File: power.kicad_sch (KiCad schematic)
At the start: 42 parts, among them U5 RT8097AHGE, U6 RT8097AHGE, U7 RT9080-28GJ5, U8 RT9080-18GJ5, U9 RT9080-12GJ5

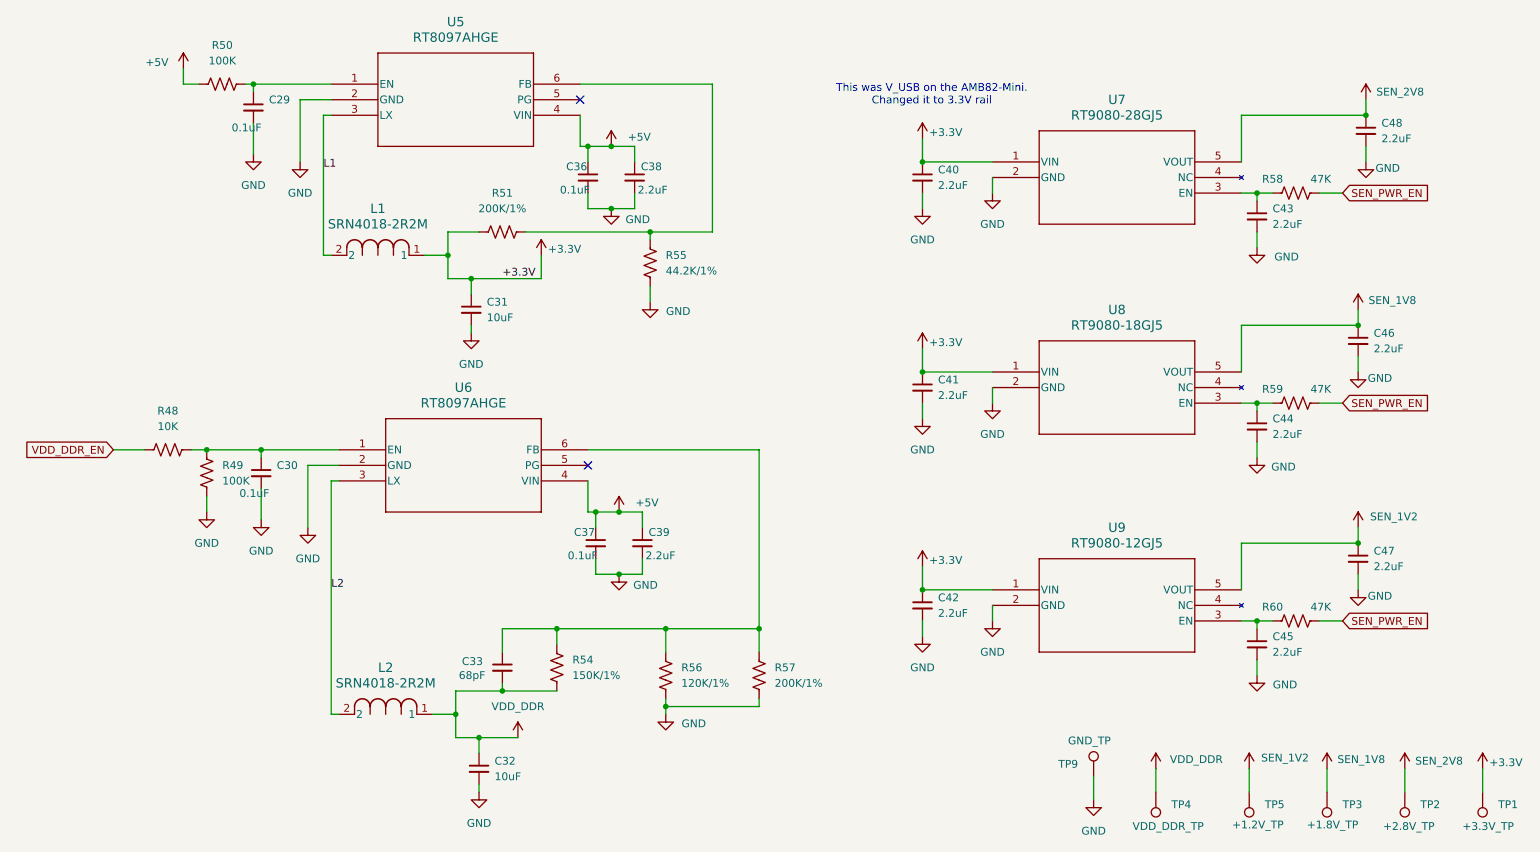
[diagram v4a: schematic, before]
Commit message: Replaced all passive footprints from 0603 metric to 0603 imperial. Big oversight. All done. Next is DRC
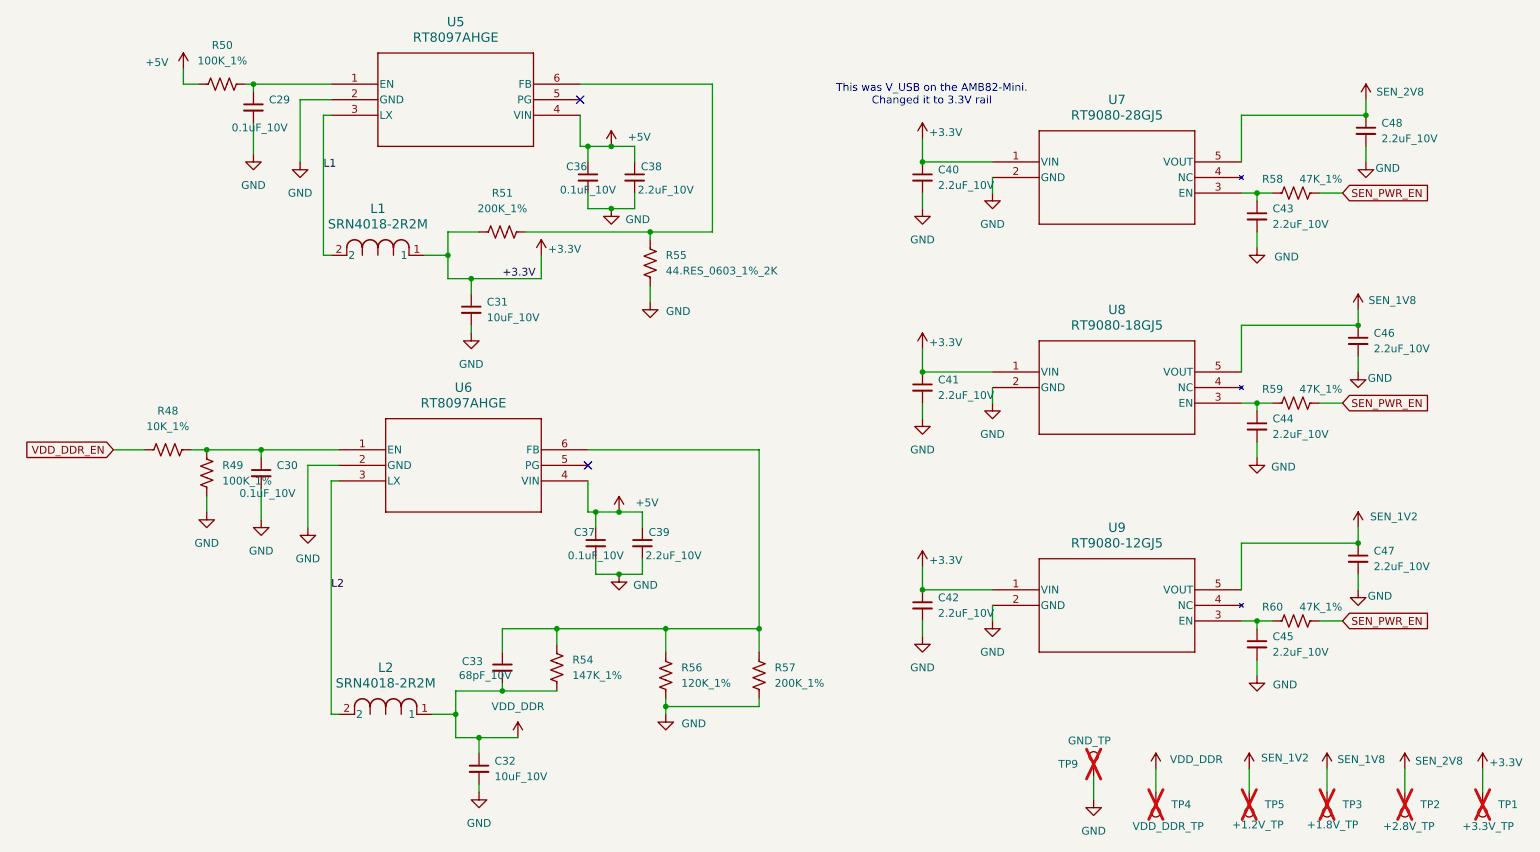
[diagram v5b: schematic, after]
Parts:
- C29, C30, C36, C37: value 0.1uF -> 0.1uF_10V; footprint Capacitor_SMD:C_0201_0603Metric_Pad0.64x0.40mm_HandSolder -> Capacitor_SMD:C_0603_1608Metric
- C31, C32: value 10uF -> 10uF_10V; footprint Capacitor_SMD:C_0201_0603Metric_Pad0.64x0.40mm_HandSolder -> Capacitor_SMD:C_0603_1608Metric
- C33: value 68pF -> 68pF_10V; footprint Capacitor_SMD:C_0201_0603Metric_Pad0.64x0.40mm_HandSolder -> Capacitor_SMD:C_0603_1608Metric
- C38, C39, C40, C41, C42, C43, C44, C45, C46, C47, C48: value 2.2uF -> 2.2uF_10V; footprint Capacitor_SMD:C_0201_0603Metric_Pad0.64x0.40mm_HandSolder -> Capacitor_SMD:C_0603_1608Metric
- R48: value 10K -> 10K_1%; footprint Resistor_SMD:R_0201_0603Metric_Pad0.64x0.40mm_HandSolder -> Resistor_SMD:R_0603_1608Metric
- R49, R50: value 100K -> 100K_1%; footprint Resistor_SMD:R_0201_0603Metric_Pad0.64x0.40mm_HandSolder -> Resistor_SMD:R_0603_1608Metric
- R51, R57: value 200K/1% -> 200K_1%; footprint Resistor_SMD:R_0201_0603Metric_Pad0.64x0.40mm_HandSolder -> Resistor_SMD:R_0603_1608Metric
- R54: value 150K/1% -> 147K_1%; footprint Resistor_SMD:R_0201_0603Metric_Pad0.64x0.40mm_HandSolder -> Resistor_SMD:R_0603_1608Metric
- R55: value 44.2K/1% -> 44.RES_0603_1%_2K; footprint Resistor_SMD:R_0201_0603Metric_Pad0.64x0.40mm_HandSolder -> Resistor_SMD:R_0603_1608Metric
- R56: value 120K/1% -> 120K_1%; footprint Resistor_SMD:R_0201_0603Metric_Pad0.64x0.40mm_HandSolder -> Resistor_SMD:R_0603_1608Metric
- R58, R59, R60: value 47K -> 47K_1%; footprint Resistor_SMD:R_0201_0603Metric_Pad0.64x0.40mm_HandSolder -> Resistor_SMD:R_0603_1608Metric
- TP1, TP2, TP3, TP4, TP5, TP9: now not fitted
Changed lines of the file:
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@@
 			)
 		)
-		(property "Value" "0.1uF"
+		(property "Value" "0.1uF_10V"
 			(at 51.054 101.092 0)
 			(effects
@@
 			)
 		)
-		(property "Footprint" "Capacitor_SMD:C_0201_0603Metric_Pad0.64x0.40mm_HandSolder"
+		(property "Footprint" "Capacitor_SMD:C_0603_1608Metric"
 			(at 54.61 97.79 0)
 			(effects
@@
 		(in_bom yes)
 		(on_board yes)
-		(dnp no)
+		(dnp yes)
 		(property "Reference" "TP2"
 			(at 243.84 151.8919 0)
@@
 			)
 		)
-		(property "Value" "2.2uF"
+		(property "Value" "2.2uF_10V"
 			(at 116.078 51.562 0)
 			(effects
@@
 			)
 		)
-		(property "Footprint" "Capacitor_SMD:C_0201_0603Metric_Pad0.64x0.40mm_HandSolder"
+		(property "Footprint" "Capacitor_SMD:C_0603_1608Metric"
 			(at 115.57 49.53 0)
 			(effects
@@
 		(in_bom yes)
 		(on_board yes)
-		(dnp no)
+		(dnp yes)
 		(property "Reference" "TP5"
 			(at 218.44 151.8919 0)
@@
 			)
 		)
-		(property "Value" "2.2uF"
+		(property "Value" "2.2uF_10V"
 			(at 237.49 43.1862 0)
 			(effects
@@
 			)
 		)
-		(property "Footprint" "Capacitor_SMD:C_0201_0603Metric_Pad0.64x0.40mm_HandSolder"
+		(property "Footprint" "Capacitor_SMD:C_0603_1608Metric"
 			(at 234.95 41.91 0)
 			(effects
@@
 			)
 		)
-		(property "Value" "2.2uF"
+		(property "Value" "2.2uF_10V"
 			(at 219.71 91.4462 0)
 			(effects
@@
 			)
 		)
-		(property "Footprint" "Capacitor_SMD:C_0201_0603Metric_Pad0.64x0.40mm_HandSolder"
+		(property "Footprint" "Capacitor_SMD:C_0603_1608Metric"
 			(at 217.17 90.17 0)
 			(effects
@@
 			)
 		)
-		(property "Value" "2.2uF"
+		(property "Value" "2.2uF_10V"
 			(at 236.22 113.0362 0)
 			(effects
@@
 			)
 		)
-		(property "Footprint" "Capacitor_SMD:C_0201_0603Metric_Pad0.64x0.40mm_HandSolder"
+		(property "Footprint" "Capacitor_SMD:C_0603_1608Metric"
 			(at 233.68 111.76 0)
 			(effects
@@
 			)
 		)
-		(property "Value" "10uF"
+		(property "Value" "10uF_10V"
 			(at 92.71 147.3262 0)
 			(effects
@@
 			)
 		)
-		(property "Footprint" "Capacitor_SMD:C_0201_0603Metric_Pad0.64x0.40mm_HandSolder"
+		(property "Footprint" "Capacitor_SMD:C_0603_1608Metric"
 			(at 90.17 146.05 0)
 			(effects
@@
 			)
 		)
-		(property "Value" "2.2uF"
+		(property "Value" "2.2uF_10V"
 			(at 165.1 50.8062 0)
 			(effects
@@
 			)
 		)
-		(property "Footprint" "Capacitor_SMD:C_0201_0603Metric_Pad0.64x0.40mm_HandSolder"
+		(property "Footprint" "Capacitor_SMD:C_0603_1608Metric"
 			(at 162.56 49.53 0)
 			(effects
@@
 		(in_bom yes)
 		(on_board yes)
-		(dnp no)
+		(dnp yes)
 		(property "Reference" "TP1"
 			(at 256.54 151.8919 0)
@@
 		(in_bom yes)
 		(on_board yes)
-		(dnp no)
+		(dnp yes)
 		(property "Reference" "TP9"
 			(at 187.96 145.2881 0)
@@
 			)
 		)
-		(property "Value" "2.2uF"
+		(property "Value" "2.2uF_10V"
 			(at 165.1 120.6562 0)
 			(effects
@@
 			)
 		)
-		(property "Footprint" "Capacitor_SMD:C_0201_0603Metric_Pad0.64x0.40mm_HandSolder"
+		(property "Footprint" "Capacitor_SMD:C_0603_1608Metric"
 			(at 162.56 119.38 0)
 			(effects
@@
 			)
 		)
-		(property "Value" "100K"
+		(property "Value" "100K_1%"
 			(at 48.26 30.48 90)
 			(effects
@@
 			)
 		)
-		(property "Footprint" "Resistor_SMD:R_0201_0603Metric_Pad0.64x0.40mm_HandSolder"
+		(property "Footprint" "Resistor_SMD:R_0603_1608Metric"
 			(at 48.514 33.274 90)
 			(effects
@@
 			)
 		)
-		(property "Value" "0.1uF"
+		(property "Value" "0.1uF_10V"
 			(at 103.378 51.562 0)
 			(effects
@@
 			)
 		)
-		(property "Footprint" "Capacitor_SMD:C_0201_0603Metric_Pad0.64x0.40mm_HandSolder"
+		(property "Footprint" "Capacitor_SMD:C_0603_1608Metric"
 			(at 107.95 49.53 0)
 			(effects
@@
 			)
 		)
-		(property "Value" "100K"
+		(property "Value" "100K_1%"
 			(at 48.26 99.0599 0)
 			(effects
@@
 			)
 		)
-		(property "Footprint" "Resistor_SMD:R_0201_0603Metric_Pad0.64x0.40mm_HandSolder"
+		(property "Footprint" "Resistor_SMD:R_0603_1608Metric"
 			(at 44.704 97.536 90)
 			(effects
@@
 			)
 		)
-		(property "Value" "150K/1%"
+		(property "Value" "147K_1%"
 			(at 105.41 130.8099 0)
 			(effects
@@
 			)
 		)
-		(property "Footprint" "Resistor_SMD:R_0201_0603Metric_Pad0.64x0.40mm_HandSolder"
+		(property "Footprint" "Resistor_SMD:R_0603_1608Metric"
 			(at 101.854 129.286 90)
 			(effects
@@
 		(in_bom yes)
 		(on_board yes)
-		(dnp no)
+		(dnp yes)
 		(property "Reference" "TP4"
 			(at 203.2 151.8919 0)
@@
 		(in_bom yes)
 		(on_board yes)
-		(dnp no)
+		(dnp yes)
 		(property "Reference" "TP3"
 			(at 231.14 151.8919 0)
@@
 			)
 		)
-		(property "Value" "2.2uF"
+		(property "Value" "2.2uF_10V"
 			(at 165.1 85.0962 0)
 			(effects
@@
 			)
 		)
-		(property "Footprint" "Capacitor_SMD:C_0201_0603Metric_Pad0.64x0.40mm_HandSolder"
+		(property "Footprint" "Capacitor_SMD:C_0603_1608Metric"
 			(at 162.56 83.82 0)
 			(effects
@@
 			)
 		)
-		(property "Value" "44.2K/1%"
+		(property "Value" "44.RES_0603_1%_2K"
 			(at 120.65 64.7699 0)
 			(effects
@@
 			)
 		)
-		(property "Footprint" "Resistor_SMD:R_0201_0603Metric_Pad0.64x0.40mm_HandSolder"
+		(property "Footprint" "Resistor_SMD:R_0603_1608Metric"
 			(at 119.126 63.754 90)
 			(effects
@@
 			)
 		)
-		(property "Value" "47K"
+		(property "Value" "47K_1%"
 			(at 227.584 119.634 90)
 			(effects
@@
 			)
 		)
-		(property "Footprint" "Resistor_SMD:R_0201_0603Metric_Pad0.64x0.40mm_HandSolder"
+		(property "Footprint" "Resistor_SMD:R_0603_1608Metric"
 			(at 223.774 120.904 90)
 			(effects
@@
 			)
 		)
-		(property "Value" "2.2uF"
+		(property "Value" "2.2uF_10V"
 			(at 236.22 77.4762 0)
 			(effects
@@
 			)
 		)
-		(property "Footprint" "Capacitor_SMD:C_0201_0603Metric_Pad0.64x0.40mm_HandSolder"
+		(property "Footprint" "Capacitor_SMD:C_0603_1608Metric"
 			(at 233.68 76.2 0)
 			(effects
@@
 			)
 		)
-		(property "Value" "47K"
+		(property "Value" "47K_1%"
 			(at 227.584 49.784 90)
 			(effects
@@
 			)
 		)
-		(property "Footprint" "Resistor_SMD:R_0201_0603Metric_Pad0.64x0.40mm_HandSolder"
+		(property "Footprint" "Resistor_SMD:R_0603_1608Metric"
 			(at 223.774 51.054 90)
 			(effects
@@
 			)
 		)
-		(property "Value" "10uF"
+		(property "Value" "10uF_10V"
 			(at 91.44 72.3962 0)
 			(effects
@@
 			)
 		)
-		(property "Footprint" "Capacitor_SMD:C_0201_0603Metric_Pad0.64x0.40mm_HandSolder"
+		(property "Footprint" "Capacitor_SMD:C_0603_1608Metric"
 			(at 88.9 71.12 0)
 			(effects
@@
 			)
 		)
-		(property "Value" "2.2uF"
+		(property "Value" "2.2uF_10V"
 			(at 219.71 57.1562 0)
 			(effects
@@
 			)
 		)
-		(property "Footprint" "Capacitor_SMD:C_0201_0603Metric_Pad0.64x0.40mm_HandSolder"
+		(property "Footprint" "Capacitor_SMD:C_0603_1608Metric"
 			(at 217.17 55.88 0)
 			(effects
@@
 			)
 		)
-		(property "Value" "0.1uF"
+		(property "Value" "0.1uF_10V"
 			(at 49.784 41.402 0)
 			(effects
@@
 			)
 		)
-		(property "Footprint" "Capacitor_SMD:C_0201_0603Metric_Pad0.64x0.40mm_HandSolder"
+		(property "Footprint" "Capacitor_SMD:C_0603_1608Metric"
 			(at 53.34 38.1 0)
 			(effects
@@
 			)
 		)
-		(property "Value" "2.2uF"
+		(property "Value" "2.2uF_10V"
 			(at 219.71 127.0062 0)
 			(effects
@@
 			)
 		)
-		(property "Footprint" "Capacitor_SMD:C_0201_0603Metric_Pad0.64x0.40mm_HandSolder"
+		(property "Footprint" "Capacitor_SMD:C_0603_1608Metric"
 			(at 217.17 125.73 0)
 			(effects
@@
 			)
 		)
-		(property "Value" "47K"
+		(property "Value" "47K_1%"
 			(at 227.584 84.074 90)
 			(effects
@@
 			)
 		)
-		(property "Footprint" "Resistor_SMD:R_0201_0603Metric_Pad0.64x0.40mm_HandSolder"
+		(property "Footprint" "Resistor_SMD:R_0603_1608Metric"
 			(at 223.774 85.344 90)
 			(effects
@@
 			)
 		)
-		(property "Value" "200K/1%"
+		(property "Value" "200K_1%"
 			(at 93.98 54.61 90)
 			(effects
@@
 			)
 		)
-		(property "Footprint" "Resistor_SMD:R_0201_0603Metric_Pad0.64x0.40mm_HandSolder"
+		(property "Footprint" "Resistor_SMD:R_0603_1608Metric"
 			(at 94.234 57.404 90)
 			(effects
@@
 			)
 		)
-		(property "Value" "10K"
+		(property "Value" "10K_1%"
 			(at 39.37 90.17 90)
 			(effects
@@
 			)
 		)
-		(property "Footprint" "Resistor_SMD:R_0201_0603Metric_Pad0.64x0.40mm_HandSolder"
+		(property "Footprint" "Resistor_SMD:R_0603_1608Metric"
 			(at 39.624 92.964 90)
 			(effects
@@
 			)
 		)
-		(property "Value" "2.2uF"
+		(property "Value" "2.2uF_10V"
 			(at 117.348 111.252 0)
 			(effects
@@
 			)
 		)
-		(property "Footprint" "Capacitor_SMD:C_0201_0603Metric_Pad0.64x0.40mm_HandSolder"
+		(property "Footprint" "Capacitor_SMD:C_0603_1608Metric"
 			(at 116.84 109.22 0)
 			(effects
@@
 			)
 		)
-		(property "Value" "0.1uF"
+		(property "Value" "0.1uF_10V"
 			(at 104.648 111.252 0)
 			(effects
@@
 			)
 		)
-		(property "Footprint" "Capacitor_SMD:C_0201_0603Metric_Pad0.64x0.40mm_HandSolder"
+		(property "Footprint" "Capacitor_SMD:C_0603_1608Metric"
 			(at 109.22 109.22 0)
 			(effects
@@
 			)
 		)
-		(property "Value" "120K/1%"
+		(property "Value" "120K_1%"
 			(at 123.19 132.0799 0)
 			(effects
@@
 			)
 		)
-		(property "Footprint" "Resistor_SMD:R_0201_0603Metric_Pad0.64x0.40mm_HandSolder"
+		(property "Footprint" "Resistor_SMD:R_0603_1608Metric"
 			(at 121.666 131.064 90)
 			(effects
@@
 			)
 		)
-		(property "Value" "68pF"
+		(property "Value" "68pF_10V"
 			(at 86.868 130.81 0)
 			(effects
@@
 			)
 		)
-		(property "Footprint" "Capacitor_SMD:C_0201_0603Metric_Pad0.64x0.40mm_HandSolder"
+		(property "Footprint" "Capacitor_SMD:C_0603_1608Metric"
 			(at 93.98 129.54 0)
 			(effects
@@
 			)
 		)
-		(property "Value" "200K/1%"
+		(property "Value" "200K_1%"
 			(at 138.43 132.0799 0)
 			(effects
@@
 			)
 		)
-		(property "Footprint" "Resistor_SMD:R_0201_0603Metric_Pad0.64x0.40mm_HandSolder"
+		(property "Footprint" "Resistor_SMD:R_0603_1608Metric"
 			(at 136.906 131.064 90)
 			(effects

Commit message: All fiducials and mounting holes placed. Except one hole, which I'll try to place. WIP
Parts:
- L1, L2: footprint IND_BOURNS_SRN4018 -> SRN4018-2R2M:IND_BOURNS_SRN4018
- U7, U8, U9: footprint TSOT-23-5_RIT -> RTL9080:TSOT-23-5_RIT
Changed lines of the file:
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@@
 			)
 		)
-		(property "Footprint" "IND_BOURNS_SRN4018"
+		(property "Footprint" "SRN4018-2R2M:IND_BOURNS_SRN4018"
 			(at 66.04 62.23 0)
 			(effects
@@
 			)
 		)
-		(property "Footprint" "IND_BOURNS_SRN4018"
+		(property "Footprint" "SRN4018-2R2M:IND_BOURNS_SRN4018"
 			(at 67.31 137.16 0)
 			(effects
@@
 			)
 		)
-		(property "Footprint" "TSOT-23-5_RIT"
+		(property "Footprint" "RTL9080:TSOT-23-5_RIT"
 			(at 173.99 46.99 0)
 			(effects
@@
 			)
 		)
-		(property "Footprint" "TSOT-23-5_RIT"
+		(property "Footprint" "RTL9080:TSOT-23-5_RIT"
 			(at 173.99 116.84 0)
 			(effects
@@
 			)
 		)
-		(property "Footprint" "TSOT-23-5_RIT"
+		(property "Footprint" "RTL9080:TSOT-23-5_RIT"
 			(at 173.99 81.28 0)
 			(effects

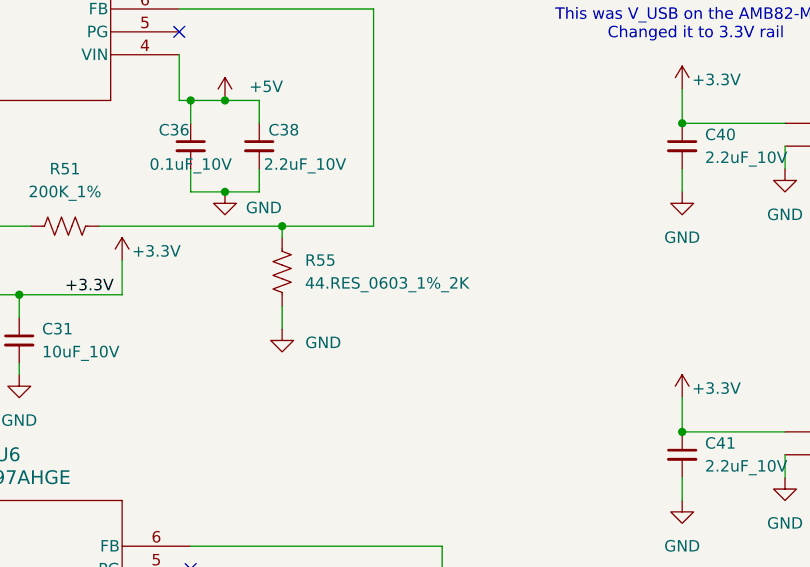
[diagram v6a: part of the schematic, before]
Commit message: Fixed R55 value
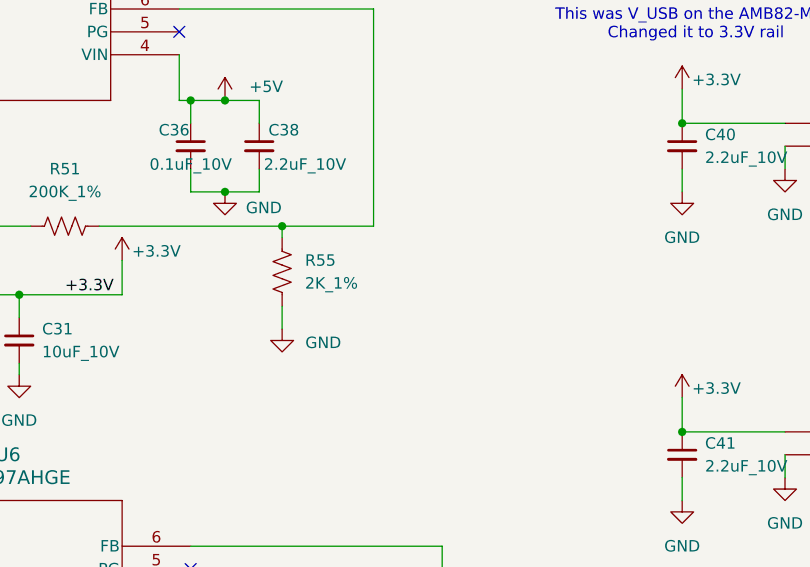
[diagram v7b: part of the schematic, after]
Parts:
- R55: value 44.RES_0603_1%_2K -> 2K_1%
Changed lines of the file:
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@@
 			)
 		)
-		(property "Value" "44.RES_0603_1%_2K"
+		(property "Value" "2K_1%"
 			(at 120.65 64.7699 0)
 			(effects
